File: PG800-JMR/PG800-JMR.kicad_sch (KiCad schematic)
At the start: 51 parts, among them J1 DIN-6, J10 POT_POWER_2, J11 POT_POWER_3, J2 POT_CENTERS_1, J3 POT_CENTERS_2, J4 POT_CENTERS_3, J5 SWITCH_BLK, J6 TEENSY_PIN_BLK1, J7 TEENSY_PIN_BLK3, J8 TEENSY_PIN_BLK2, J9 POT_POWER_1, Q1 BSS138, Q2 BSS138, Q3 BSS138, U1 LM2575-5BT, U2 CD74HC4067M, U3 CD74HC4067M, U4 CD74HC4067M, U5 74HC165A

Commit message: updated kicad drawings, tweaked code slightly
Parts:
- added J12: GND_BLK, Connector_PinHeader_2.54mm:PinHeader_1x09_P2.54mm_Vertical, symbol Connector:Conn_01x09_Pin
- added J13: 3.3V_BLK, Connector_PinHeader_2.54mm:PinHeader_1x09_P2.54mm_Vertical, symbol Connector:Conn_01x09_Pin
- added J14: 5V_BLK, Connector_PinHeader_2.54mm:PinHeader_1x09_P2.54mm_Vertical, symbol Connector:Conn_01x09_Pin
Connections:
- net +5V: now also J14.1 (Pin_1), J14.2 (Pin_2), J14.3 (Pin_3), J14.4 (Pin_4), J14.5 (Pin_5), J14.6 (Pin_6), J14.7 (Pin_7), J14.8 (Pin_8), J14.9 (Pin_9)
- net 3.3V: now also J13.1 (Pin_1), J13.2 (Pin_2), J13.3 (Pin_3), J13.4 (Pin_4), J13.5 (Pin_5), J13.6 (Pin_6), J13.7 (Pin_7), J13.8 (Pin_8), J13.9 (Pin_9)
- net GND: now also J12.1 (Pin_1), J12.2 (Pin_2), J12.3 (Pin_3), J12.4 (Pin_4), J12.5 (Pin_5), J12.6 (Pin_6), J12.7 (Pin_7), J12.8 (Pin_8), J12.9 (Pin_9)

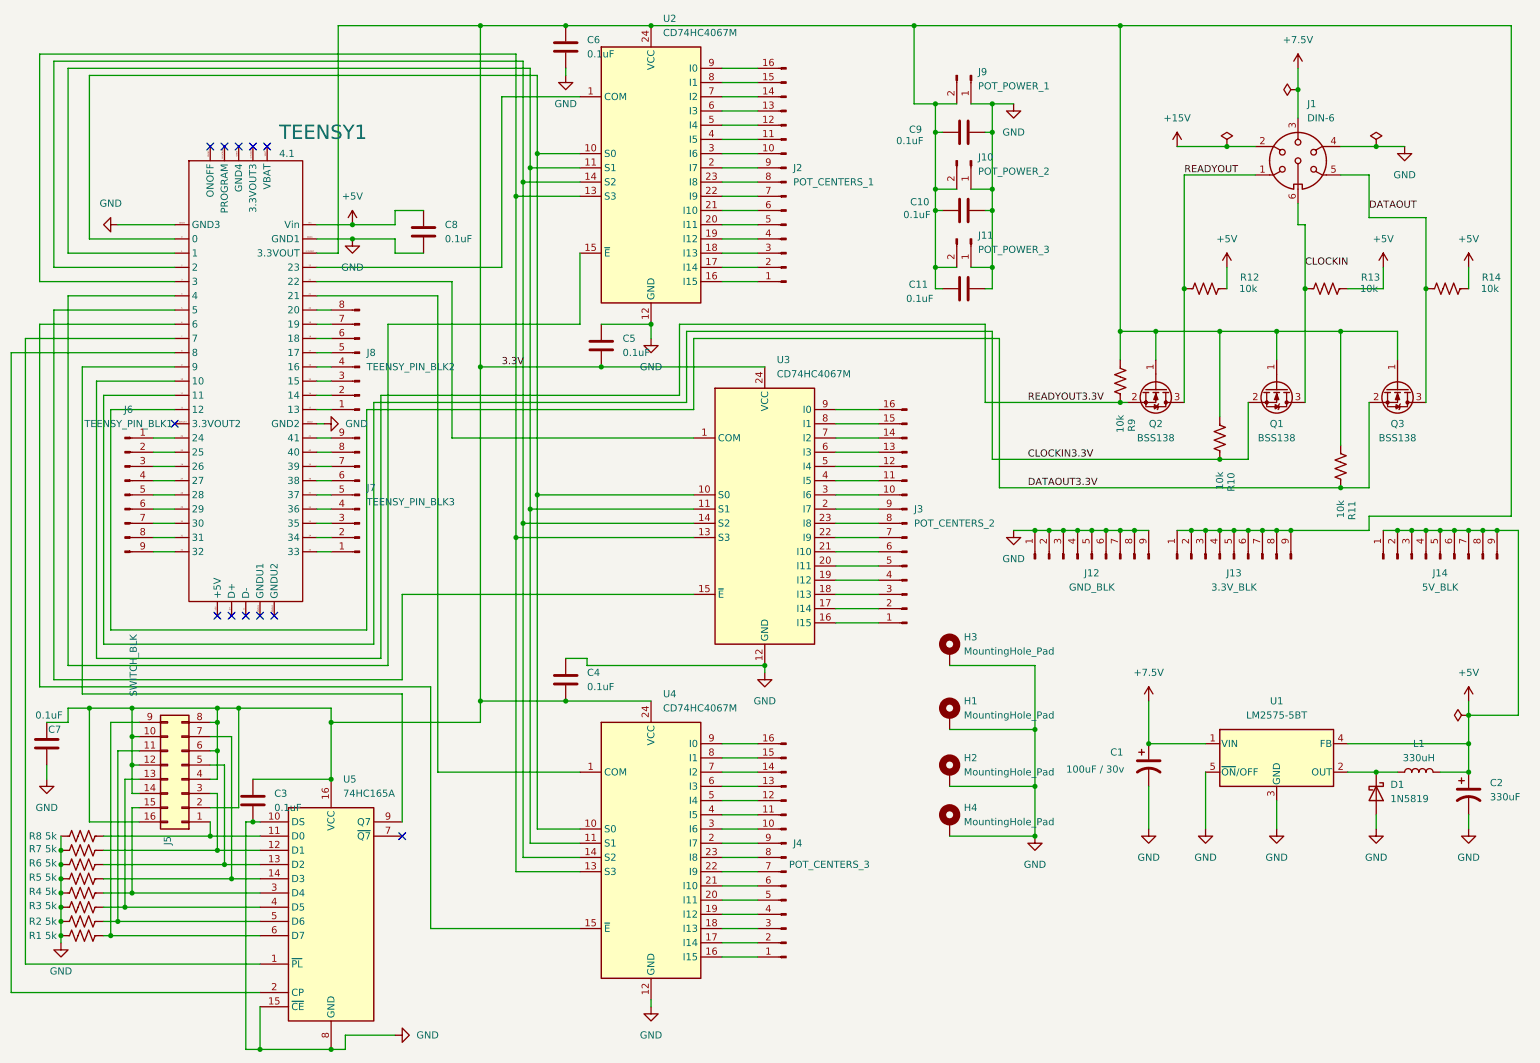
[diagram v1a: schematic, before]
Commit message: updated PCB design, added optional 3.3V regulator, added another mux
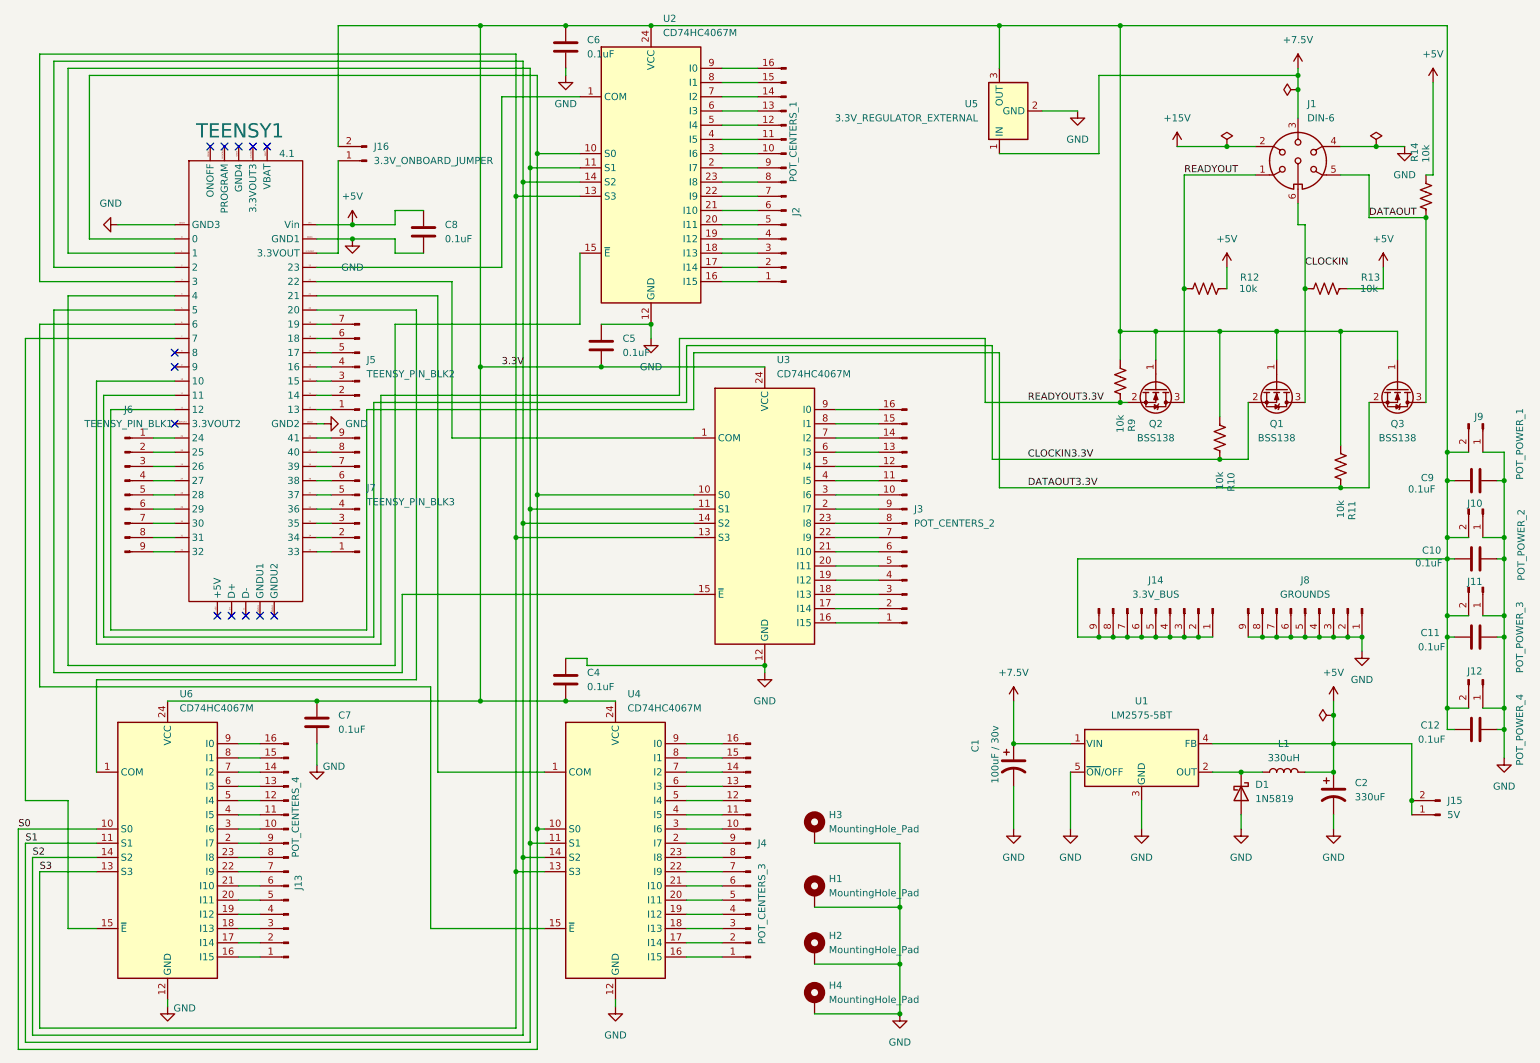
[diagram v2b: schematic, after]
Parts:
- removed C3: 0.1uF, Capacitor_THT:C_Disc_D5.0mm_W2.5mm_P2.50mm, symbol Device:C
- removed J12: GND_BLK, Connector_PinHeader_2.54mm:PinHeader_1x09_P2.54mm_Vertical, symbol Connector:Conn_01x09_Pin
- removed J13: 3.3V_BLK, Connector_PinHeader_2.54mm:PinHeader_1x09_P2.54mm_Vertical, symbol Connector:Conn_01x09_Pin
- removed J5: SWITCH_BLK, Connector_PinHeader_2.54mm:PinHeader_2x08_P2.54mm_Vertical, symbol Connector_Generic:Conn_02x08_Counter_Clockwise
- removed J8: TEENSY_PIN_BLK2, Connector_PinHeader_2.54mm:PinHeader_1x08_P2.54mm_Vertical, symbol Connector:Conn_01x08_Pin
- removed R1, R2, R3, R4, R5, R6, R7, R8: 5k, Resistor_THT:R_Axial_DIN0204_L3.6mm_D1.6mm_P7.62mm_Horizontal, symbol Device:R_US
- removed U5: 74HC165A, Package_DIP:DIP-16_W7.62mm, symbol 74xx:74HC165
- added C12: 0.1uF, Capacitor_THT:C_Disc_D5.0mm_W2.5mm_P2.50mm, symbol Device:C
- added J12: POT_POWER_4, Connector_PinHeader_2.54mm:PinHeader_1x02_P2.54mm_Vertical, symbol Connector:Conn_01x02_Pin
- added J13: POT_CENTERS_4, Connector_PinHeader_2.54mm:PinHeader_1x16_P2.54mm_Vertical, symbol Connector:Conn_01x16_Pin
- added J15: 5V, Connector_PinHeader_2.54mm:PinHeader_1x02_P2.54mm_Vertical, symbol Connector:Conn_01x02_Pin
- added J16: 3.3V_ONBOARD_JUMPER, Connector_PinHeader_2.54mm:PinHeader_1x02_P2.54mm_Vertical, symbol Connector:Conn_01x02_Pin
- added J5: TEENSY_PIN_BLK2, Connector_PinHeader_2.54mm:PinHeader_1x07_P2.54mm_Vertical, symbol Connector:Conn_01x07_Pin
- added J8: GROUNDS, Connector_PinHeader_2.54mm:PinHeader_1x09_P2.54mm_Vertical, symbol Connector:Conn_01x09_Pin
- added U5: 3.3V_REGULATOR_EXTERNAL, Converter_DCDC:Converter_DCDC_Murata_OKI-78SR_Vertical, symbol Converter_DCDC:OKI-78SR-3.3_1.5-W36-C
- added U6: CD74HC4067M, Package_SO:SOIC-24W_7.5x15.4mm_P1.27mm, symbol 74xx:CD74HC4067M
- J14: value 5V_BLK -> 3.3V_BUS
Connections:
- net +5V: now also J15.1 (Pin_1), J15.2 (Pin_2); no longer J14.1 (Pin_1), J14.2 (Pin_2), J14.3 (Pin_3), J14.4 (Pin_4), J14.5 (Pin_5), J14.6 (Pin_6), J14.7 (Pin_7), J14.8 (Pin_8), J14.9 (Pin_9)
- net +7.5V: now also U5.1 (IN)
- net 3.3V: now also J14.1 (Pin_1), J14.2 (Pin_2), J14.3 (Pin_3), J14.4 (Pin_4), J14.5 (Pin_5), J14.6 (Pin_6), J14.7 (Pin_7), J14.8 (Pin_8), J14.9 (Pin_9), C12.1, J12.2 (Pin_2), J16.2 (Pin_2), U5.3 (OUT), U6.24 (VCC); no longer TEENSY1.3.3VOUT
- net GND: now also C12.2, J12.1 (Pin_1), J8.1 (Pin_1), J8.2 (Pin_2), J8.3 (Pin_3), J8.4 (Pin_4), J8.5 (Pin_5), J8.6 (Pin_6), J8.7 (Pin_7), J8.8 (Pin_8), J8.9 (Pin_9), U5.2 (GND), U6.12 (GND)
- net S0: now reaches TEENSY1.0, U2.10 (S0), U3.10 (S0), U4.10 (S0)
- net S0: now also U6.10 (S0)
- net S1: now reaches TEENSY1.1, U2.11 (S1), U3.11 (S1), U4.11 (S1)
- net S1: now also U6.11 (S1)
- net at TEENSY1.13: now also J5.1 (Pin_1)
- net at TEENSY1.14: now also J5.2 (Pin_2)
- net at TEENSY1.15: now also J5.3 (Pin_3)
- net at TEENSY1.16: now also J5.4 (Pin_4)
- net at TEENSY1.17: now also J5.5 (Pin_5)
- net at TEENSY1.18: now also J5.6 (Pin_6)
- net at TEENSY1.19: now also J5.7 (Pin_7)
- net S2: now reaches TEENSY1.2, U2.14 (S2), U3.14 (S2), U4.14 (S2)
- net S2: now also U6.14 (S2)
- net at TEENSY1.20: now also U6.1 (COM)
- net S3: now reaches TEENSY1.3, U2.13 (S3), U3.13 (S3), U4.13 (S3)
- net S3: now also U6.13 (S3)
- net at TEENSY1.7: now also U6.15 (~{E})
- new net: J16.1 (Pin_1), TEENSY1.3.3VOUT
- new net: J13.1 (Pin_1), U6.16 (I15)
- new net: J13.2 (Pin_2), U6.17 (I14)
- new net: J13.3 (Pin_3), U6.18 (I13)
- new net: J13.4 (Pin_4), U6.19 (I12)
- new net: J13.9 (Pin_9), U6.2 (I7)
- new net: J13.5 (Pin_5), U6.20 (I11)
- new net: J13.6 (Pin_6), U6.21 (I10)
- new net: J13.7 (Pin_7), U6.22 (I9)
- new net: J13.8 (Pin_8), U6.23 (I8)
- new net: J13.10 (Pin_10), U6.3 (I6)
- new net: J13.11 (Pin_11), U6.4 (I5)
- new net: J13.12 (Pin_12), U6.5 (I4)
- new net: J13.13 (Pin_13), U6.6 (I3)
- new net: J13.14 (Pin_14), U6.7 (I2)
- new net: J13.15 (Pin_15), U6.8 (I1)
- new net: J13.16 (Pin_16), U6.9 (I0)
- no-connect marks 12 -> 13
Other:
- moved on the sheet: C1, C10, C11, C2, C9, D1, H1, H2, H3, H4, J10, J11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

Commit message: updated 3d image
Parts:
- removed J6: TEENSY_PIN_BLK1, Connector_PinHeader_2.54mm:PinHeader_1x09_P2.54mm_Vertical, symbol Connector:Conn_01x09_Pin
- added C13: 0.1uF, Capacitor_THT:C_Disc_D5.0mm_W2.5mm_P2.50mm, symbol Device:C
- added J17: LED_REG_CONN, Connector_PinHeader_2.54mm:PinHeader_1x08_P2.54mm_Vertical, symbol Connector:Conn_01x08_Pin
- added J6: TEENSY_PIN_BLK1, Connector_PinHeader_2.54mm:PinHeader_1x06_P2.54mm_Vertical, symbol Connector:Conn_01x06_Pin
- added R1, R2, R3, R4, R5, R6, R7, R8: 220, Resistor_THT:R_Axial_DIN0204_L3.6mm_D1.6mm_P2.54mm_Vertical, symbol Device:R_US
- added R15: 720, Resistor_THT:R_Axial_DIN0204_L3.6mm_D1.6mm_P2.54mm_Vertical, symbol Device:R_US
- added U7: 74HC595, Package_DIP:DIP-16_W7.62mm, symbol 74xx:74HC595
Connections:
- net 3.3V: now also C4.1, C13.1, U7.10 (~{SRCLR}), U7.16 (VCC); no longer C4.2
- net CLOCKIN: now also R15.1
- net GND: now also C4.2, C13.2, R15.2, U7.13 (~{OE}), U7.8 (GND); no longer C4.1
- net at TEENSY1.24: now also J6.1 (Pin_1)
- net at TEENSY1.25: now also J6.2 (Pin_2)
- net at TEENSY1.26: now also J6.3 (Pin_3)
- net at TEENSY1.27: now also J6.4 (Pin_4)
- net at TEENSY1.28: now also J6.5 (Pin_5)
- net at TEENSY1.29: now also J6.6 (Pin_6)
- net at TEENSY1.30: now also U7.12 (RCLK)
- net at TEENSY1.31: now also U7.11 (SRCLK)
- net at TEENSY1.32: now also U7.14 (SER)
- new net: R5.1, U7.4 (QE)
- new net: J17.4 (Pin_4), R5.2
- new net: R1.1, U7.15 (QA)
- new net: J17.8 (Pin_8), R1.2
- new net: R2.1, U7.1 (QB)
- new net: J17.7 (Pin_7), R2.2
- new net: R6.1, U7.5 (QF)
- new net: J17.3 (Pin_3), R6.2
- new net: R7.1, U7.6 (QG)
- new net: J17.2 (Pin_2), R7.2
- new net: R3.1, U7.2 (QC)
- new net: J17.6 (Pin_6), R3.2
- new net: R4.1, U7.3 (QD)
- new net: R8.1, U7.7 (QH)
- new net: J17.1 (Pin_1), R8.2
- new net: J17.5 (Pin_5), R4.2
- no-connect marks 13 -> 14
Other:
- moved on the sheet: C4, U5

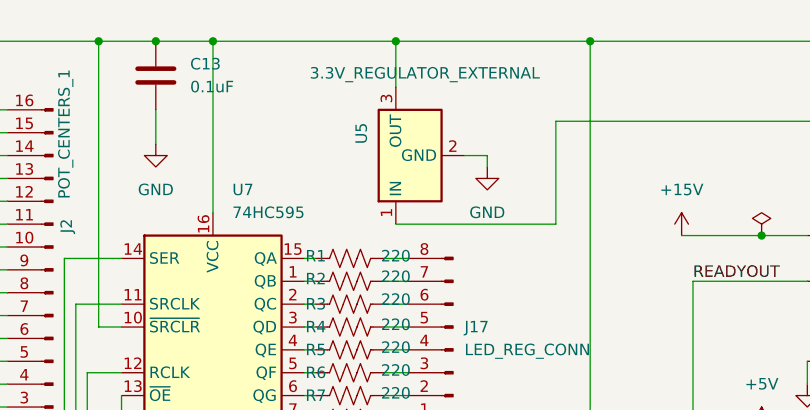
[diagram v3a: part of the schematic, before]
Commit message: Fixed LM1117-3.3, pins in wrong order
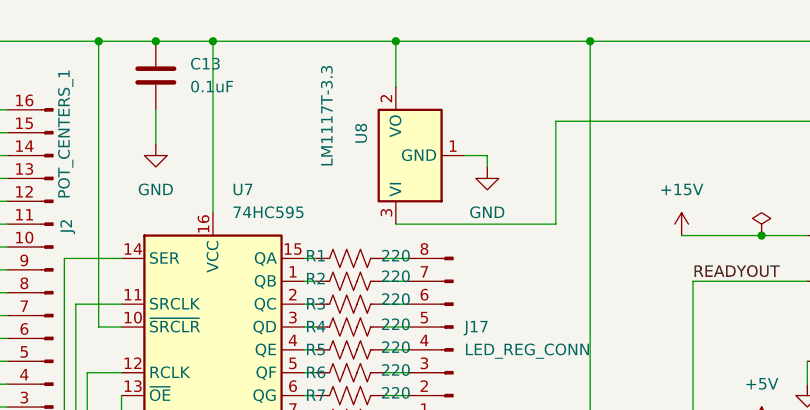
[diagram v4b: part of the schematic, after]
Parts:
- removed U5: 3.3V_REGULATOR_EXTERNAL, Converter_DCDC:Converter_DCDC_Murata_OKI-78SR_Vertical, symbol Converter_DCDC:OKI-78SR-3.3_1.5-W36-C
- added U8: LM1117T-3.3, Package_TO_SOT_THT:TO-220-3_Vertical, symbol Regulator_Linear:LM1117T-3.3
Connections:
- net +7.5V: now also U8.3 (VI)
- net 3.3V: now also U8.2 (VO)
- net GND: now also U8.1 (GND)
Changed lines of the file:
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@@
 	(title_block
 		(title "Roland JX8P Controller Board")
-		(date "2025-04-07")
-		(rev "0.3")
+		(date "2025-04-25")
+		(rev "0.4")
 		(company "SoftObject Systems")
 	)
@@
 	)
 	(symbol
-		(lib_id "Converter_DCDC:OKI-78SR-3.3_1.5-W36-C")
-		(at 189.23 26.67 90)
-		(unit 1)
-		(exclude_from_sim no)
-		(in_bom yes)
-		(on_board yes)
-		(dnp no)
-		(property "Reference" "U5"
-			(at 185.42 25.3999 0)
-			(effects
-				(font
-					(size 1.27 1.27)
-				)
-				(justify left)
-			)
-		)
-		(property "Value" "3.3V_REGULATOR_EXTERNAL"
-			(at 205.232 17.526 90)
-			(effects
-				(font
-					(size 1.27 1.27)
-				)
-				(justify left)
-			)
-		)
-		(property "Footprint" "Converter_DCDC:Converter_DCDC_Murata_OKI-78SR_Vertical"
-			(at 195.58 25.4 0)
-			(effects
-				(font
-					(size 1.27 1.27)
-					(italic yes)
-				)
-				(justify left)
-				(hide yes)
-			)
-		)
-		(property "Datasheet" "https://power.murata.com/data/power/oki-78sr.pdf"
-			(at 189.23 26.67 0)
-			(effects
-				(font
-					(size 1.27 1.27)
-				)
-				(hide yes)
-			)
-		)
-		(property "Description" "1.5A Step-Down DC/DC-Regulator, 7-36V input, 3.3V fixed Output Voltage, LM78xx replacement, -40°C to +85°C, OKI-78SR_Vertical"
-			(at 189.23 26.67 0)
-			(effects
-				(font
-					(size 1.27 1.27)
-				)
-				(hide yes)
-			)
-		)
-		(pin "1"
-		)
-		(pin "3"
-		)
-		(pin "2"
-		)
-		(instances
-			(project ""
-				(path "/07dc1f8f-157a-49ca-b986-2f6d77e4e419"
-					(reference "U5")
-					(unit 1)
-				)
-			)
-		)
-	)
-	(symbol
 		(lib_id "Device:C")
 		(at 118.11 71.12 0)
@@
 					(unit 1)
 				)
+			)
+		)
+	)
+	(symbol
+		(lib_id "Regulator_Linear:LM1117T-3.3")
+		(at 189.23 26.67 90)
+		(unit 1)
+		(exclude_from_sim no)
+		(in_bom yes)
+		(on_board yes)
+		(dnp no)
+		(property "Reference" "U8"
+			(at 185.42 25.3999 0)
+			(effects
+				(font
+					(size 1.27 1.27)
+				)
+				(justify left)
+			)
+		)
+		(property "Value" "LM1117T-3.3"
+			(at 181.61 27.94 0)
+			(effects
+				(font
+					(size 1.27 1.27)
+				)
+				(justify left)
+			)
+		)
+		(property "Footprint" "Package_TO_SOT_THT:TO-220-3_Vertical"
+			(at 189.23 26.67 0)
+			(effects
+				(font
+					(size 1.27 1.27)
+				)
+				(hide yes)
+			)
+		)
+		(property "Datasheet" "http://www.ti.com/lit/ds/symlink/lm1117.pdf"
+			(at 189.23 26.67 0)
+			(effects
+				(font
+					(size 1.27 1.27)
+				)
+				(hide yes)
+			)
+		)
+		(property "Description" "800mA Low-Dropout Linear Regulator, 3.3V fixed output, TO-220"
+			(at 189.23 26.67 0)
+			(effects
+				(font
+					(size 1.27 1.27)
+				)
+				(hide yes)
+			)
+		)
+		(pin "2"
+		)
+		(pin "1"
+		)
+		(pin "3"
+		)
+		(instances
+			(project ""
+				(path "/07dc1f8f-157a-49ca-b986-2f6d77e4e419"
+					(reference "U8")
+					(unit 1)
+				)
